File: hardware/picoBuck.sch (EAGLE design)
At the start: 23 parts, among them U1 AL8805, U2 AL8805, U3 AL8805

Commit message: Bringing up to standards- submitting this for review
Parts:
- added FRAME1: FRAME-LETTER, SparkFun-Aesthetics:FRAME-LETTER
- added LOGO1: OSHW-LOGOS, SparkFun-Aesthetics:OSHW-LOGOS
- added LOGO2: LOGO-SFENEW, SparkFun-Aesthetics:LOGO-SFENEW
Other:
- note added: "01"
- note removed: "PicoBuck"
- moved on the sheet: C1, C2, C3, C4, C5, C6, CH1, CH2, CH3, D1, D2, D3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

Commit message: Tweaks on text positions.
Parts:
- removed JP1: (no value), SparkFun:M03SCREW_LOCK
- added JP3, JP4: M022.54MM_SCREWTERM, SparkFun-Connectors:M022.54MM_SCREWTERM
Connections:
- net CTRL_CH1: now also JP4.1; no longer JP1.3
- net CTRL_CH2: now also JP3.2; no longer JP1.2
- net CTRL_CH3: now also JP3.1; no longer JP1.1
- net GND: now also JP4.2
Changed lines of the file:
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@@
 <part name="L3" library="Protofusion" deviceset="SRN6045" device=""/>
 <part name="JP2" library="SparkFun" deviceset="M02" device="3.5MM_LOCK"/>
-<part name="JP1" library="SparkFun" deviceset="M03" device="SCREW_LOCK"/>
 <part name="CH2" library="SparkFun" deviceset="M02" device="3.5MM_LOCK"/>
 <part name="CH1" library="SparkFun" deviceset="M02" device="3.5MM_LOCK"/>
@@
 <part name="LOGO2" library="SparkFun-Aesthetics" deviceset="LOGO-SFE" device="NEW"/>
 <part name="FRAME1" library="SparkFun-Aesthetics" deviceset="FRAME-LETTER" device=""/>
+<part name="JP3" library="SparkFun-Connectors" deviceset="M02" device="2.54MM_SCREWTERM" value="M022.54MM_SCREWTERM"/>
+<part name="JP4" library="SparkFun-Connectors" deviceset="M02" device="2.54MM_SCREWTERM" value="M022.54MM_SCREWTERM"/>
 </parts>
 <sheets>
@@
 <instance part="L3" gate="G$1" x="203.2" y="121.92" rot="R90"/>
 <instance part="JP2" gate="G$1" x="111.76" y="55.88" rot="R180"/>
-<instance part="JP1" gate="G$1" x="111.76" y="68.58" rot="R180"/>
 <instance part="CH2" gate="G$1" x="142.24" y="137.16" rot="R180"/>
 <instance part="CH1" gate="G$1" x="63.5" y="137.16" rot="R180"/>
@@
 <instance part="FRAME1" gate="G$1" x="0" y="0"/>
 <instance part="FRAME1" gate="G$2" x="147.32" y="0"/>
+<instance part="JP3" gate="G$1" x="111.76" y="81.28" smashed="yes" rot="R180">
+<attribute name="NAME" x="114.3" y="75.438" size="1.778" layer="95" rot="R180"/>
+</instance>
+<instance part="JP4" gate="G$1" x="111.76" y="68.58" smashed="yes" rot="R180">
+<attribute name="NAME" x="114.3" y="62.738" size="1.778" layer="95" rot="R180"/>
+</instance>
 </instances>
 <busses>
 </busses>
 <nets>
-<net name="GND" class="1">
+<net name="GND" class="0">
 <segment>
 <pinref part="U2" gate="G$1" pin="GND"/>
@@
 <segment>
 <pinref part="JP2" gate="G$1" pin="1"/>
-<wire x1="104.14" y1="55.88" x2="93.98" y2="55.88" width="0.1524" layer="91"/>
-<label x="93.98" y="55.88" size="1.778" layer="95"/>
-</segment>
-</net>
-<net name="VIN" class="1">
+<wire x1="104.14" y1="55.88" x2="101.6" y2="55.88" width="0.1524" layer="91"/>
+<label x="101.6" y="55.88" size="1.27" layer="95" rot="R180" xref="yes"/>
+</segment>
+<segment>
+<pinref part="JP4" gate="G$1" pin="2"/>
+<wire x1="104.14" y1="66.04" x2="101.6" y2="66.04" width="0.1524" layer="91"/>
+<label x="101.6" y="66.04" size="1.27" layer="95" rot="R180" xref="yes"/>
+</segment>
+</net>
+<net name="VIN" class="0">
 <segment>
 <pinref part="U2" gate="G$1" pin="VIN"/>
@@
 <segment>
 <pinref part="JP2" gate="G$1" pin="2"/>
-<wire x1="104.14" y1="53.34" x2="93.98" y2="53.34" width="0.1524" layer="91"/>
-<label x="93.98" y="53.34" size="1.778" layer="95"/>
+<wire x1="104.14" y1="53.34" x2="101.6" y2="53.34" width="0.1524" layer="91"/>
+<label x="101.6" y="53.34" size="1.27" layer="95" rot="R180" xref="yes"/>
 </segment>
 </net>
@@
 <net name="CTRL_CH1" class="0">
 <segment>
-<pinref part="JP1" gate="G$1" pin="3"/>
-<wire x1="104.14" y1="66.04" x2="93.98" y2="66.04" width="0.1524" layer="91"/>
-<label x="91.44" y="66.04" size="1.778" layer="95"/>
-</segment>
-<segment>
 <pinref part="U1" gate="G$1" pin="CTRL"/>
 <wire x1="17.78" y1="157.48" x2="5.08" y2="157.48" width="0.1524" layer="91"/>
 <label x="5.08" y="157.48" size="1.778" layer="95"/>
 </segment>
+<segment>
+<pinref part="JP4" gate="G$1" pin="1"/>
+<wire x1="104.14" y1="68.58" x2="101.6" y2="68.58" width="0.1524" layer="91"/>
+<label x="101.6" y="68.58" size="1.27" layer="95" rot="R180" xref="yes"/>
+</segment>
 </net>
 <net name="CTRL_CH2" class="0">
-<segment>
-<pinref part="JP1" gate="G$1" pin="2"/>
-<wire x1="104.14" y1="68.58" x2="93.98" y2="68.58" width="0.1524" layer="91"/>
-<label x="91.44" y="68.58" size="1.778" layer="95"/>
-</segment>
 <segment>
 <pinref part="U2" gate="G$1" pin="CTRL"/>
@@
 <label x="83.82" y="157.48" size="1.778" layer="95"/>
 </segment>
+<segment>
+<pinref part="JP3" gate="G$1" pin="2"/>
+<wire x1="104.14" y1="78.74" x2="101.6" y2="78.74" width="0.1524" layer="91"/>
+<label x="101.6" y="78.74" size="1.27" layer="95" rot="R180" xref="yes"/>
+</segment>
 </net>
 <net name="CTRL_CH3" class="0">
-<segment>
-<pinref part="JP1" gate="G$1" pin="1"/>
-<wire x1="104.14" y1="71.12" x2="93.98" y2="71.12" width="0.1524" layer="91"/>
-<label x="91.44" y="71.12" size="1.778" layer="95"/>
-</segment>
 <segment>
 <pinref part="U3" gate="G$1" pin="CTRL"/>
@@
 <label x="162.56" y="160.02" size="1.778" layer="95"/>
 </segment>
-</net>
+<segment>
+<pinref part="JP3" gate="G$1" pin="1"/>
+<wire x1="104.14" y1="81.28" x2="101.6" y2="81.28" width="0.1524" layer="91"/>
+<label x="101.6" y="81.28" size="1.27" layer="95" rot="R180" xref="yes"/>
+</segment>
+</net>

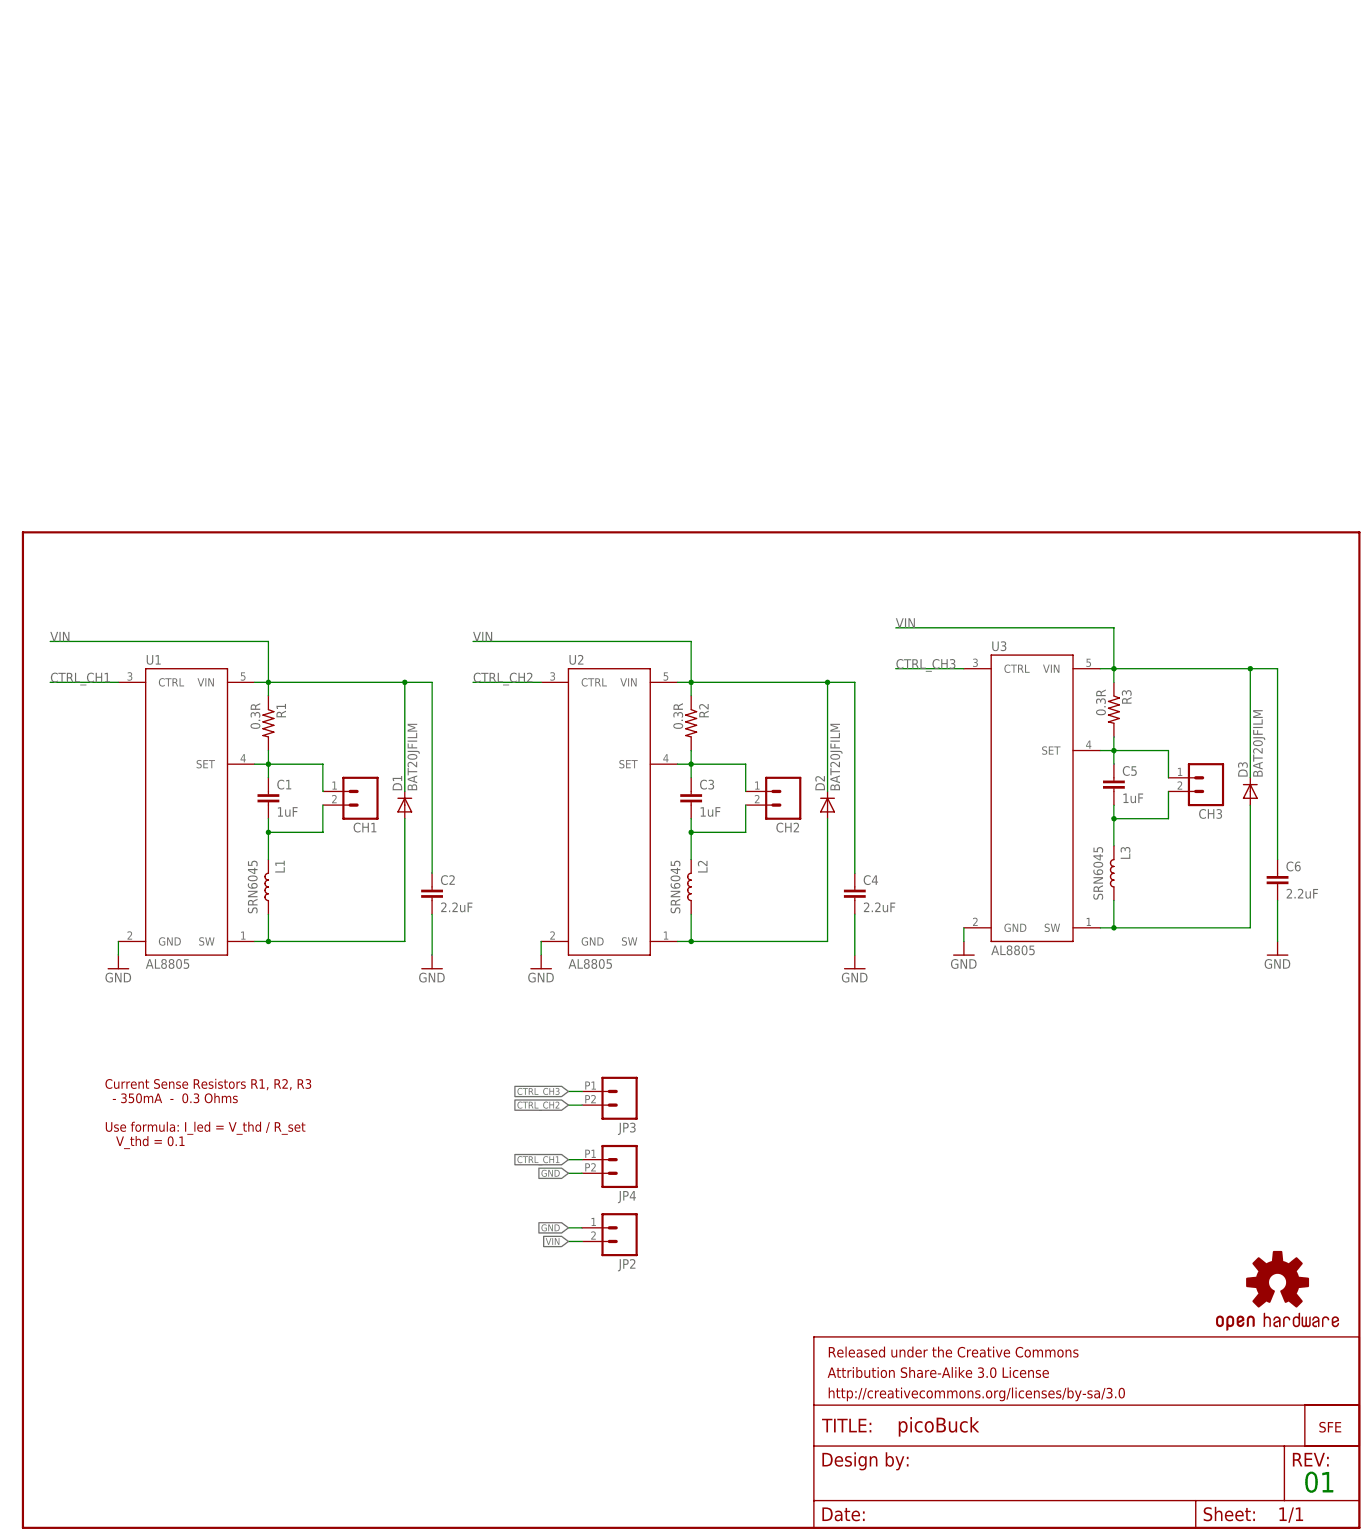
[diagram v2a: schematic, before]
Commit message: Update to v10, for release. Add .gitignore and README
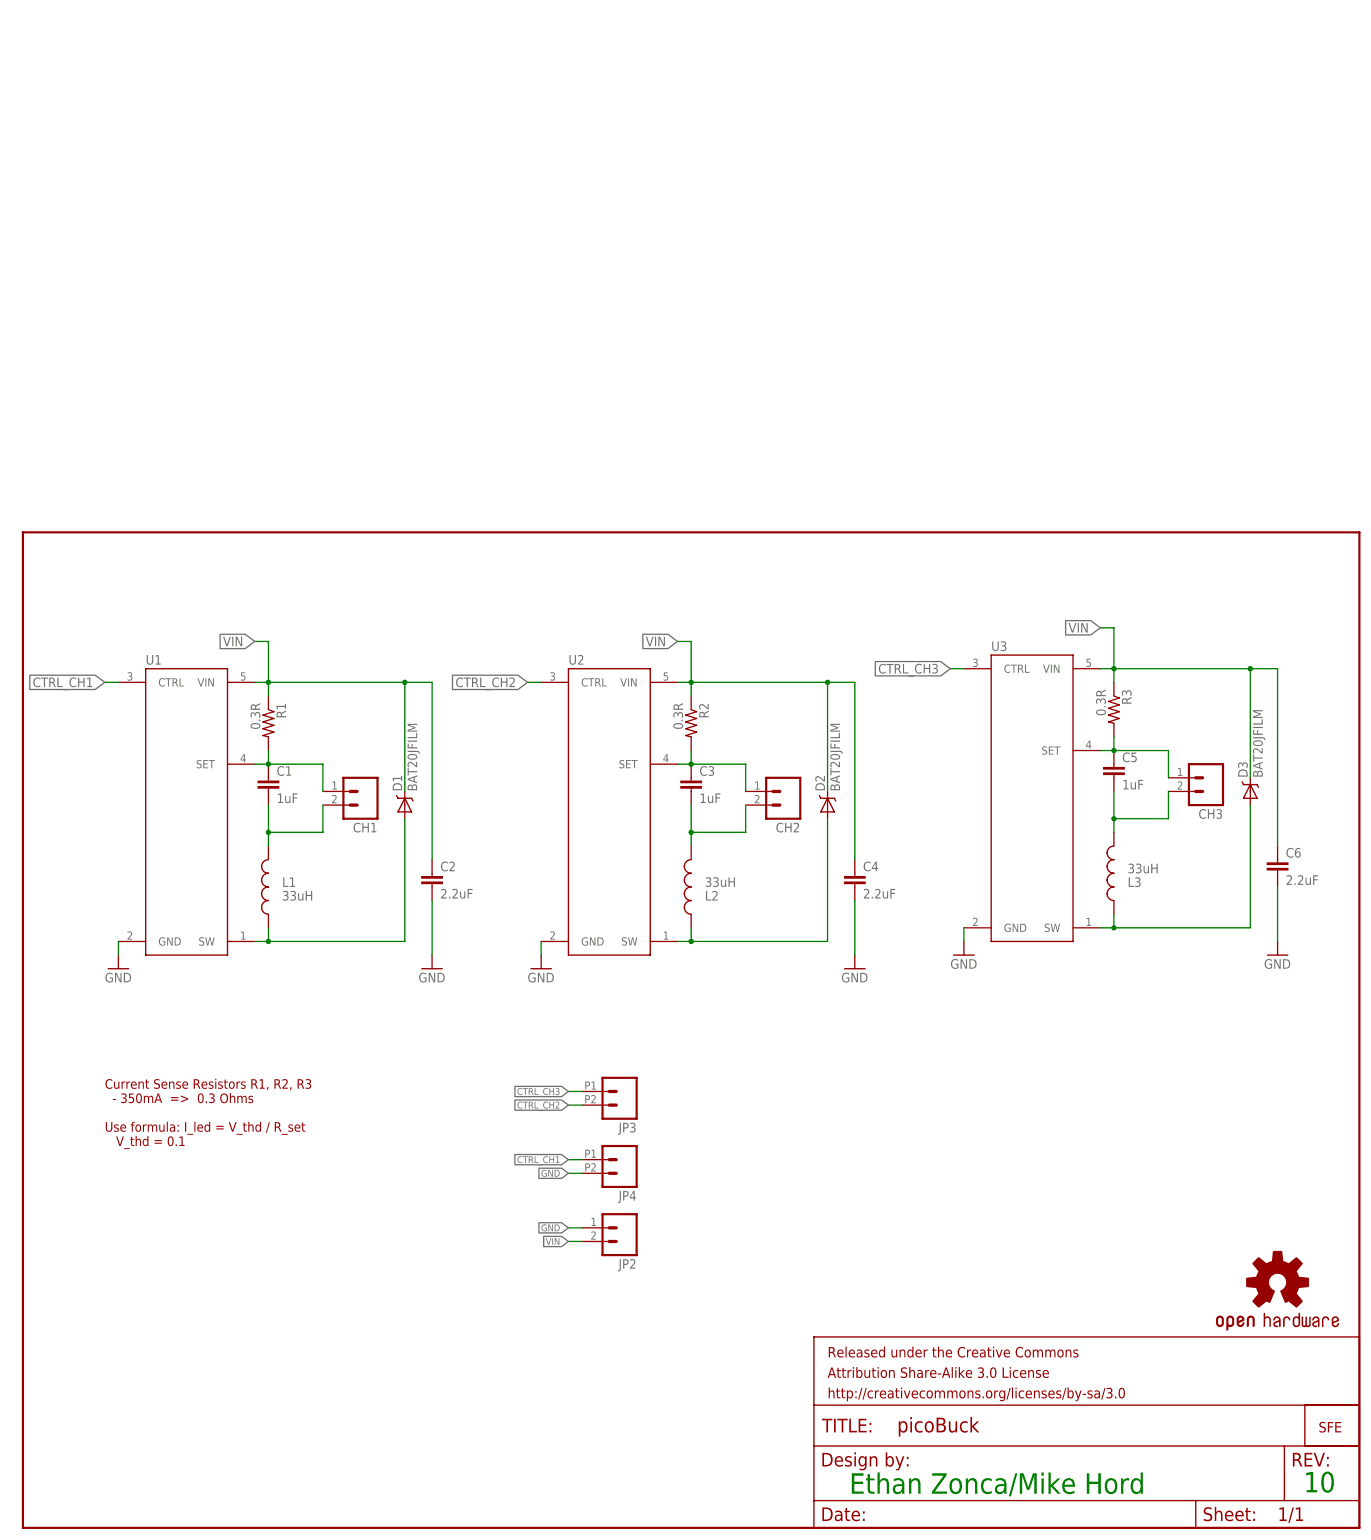
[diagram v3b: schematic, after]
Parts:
- C1, C3, C5: device resistor:C-EUC0805 -> SparkFun-Capacitors:1.0UF-25V-+80/-20(0805)
- C2, C4, C6: device resistor:C-EUC0805 -> SparkFun-Capacitors:2.2UF-25V-+80/-20(0805)
- D1, D2, D3: device SparkFun:DIODESOD -> SparkFun-DiscreteSemi:BAT20JFILM
- L1, L2, L3: value SRN6045 -> 33uH; device Protofusion:SRN6045 -> SparkFun-Passives:INDUCTORBOURNS_SRN6045
- R1, R2, R3: device resistor:R-US_R0805 -> SparkFun-Resistors:0.3OHM-1/8W-1%(0805)
- U1, U2, U3: value AL8805 -> (none); device Protofusion:AL8805 -> SparkFun-PowerIC:AL8805
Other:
- note added: "10"
- note added: "Current Sense Resistors R1, R2, R3 - 350mA => 0.3 Ohms Use formula: I_led = V_thd / R_set V_thd = 0.1"
- note added: "Ethan Zonca/Mike Hord"
- note removed: "01"
- note removed: "Current Sense Resistors R1, R2, R3 - 350mA - 0.3 Ohms Use formula: I_led = V_thd / R_set V_thd = 0.1"
- moved on the sheet: C1, C2, C3, C4, C5, C6, L1, L2, L3

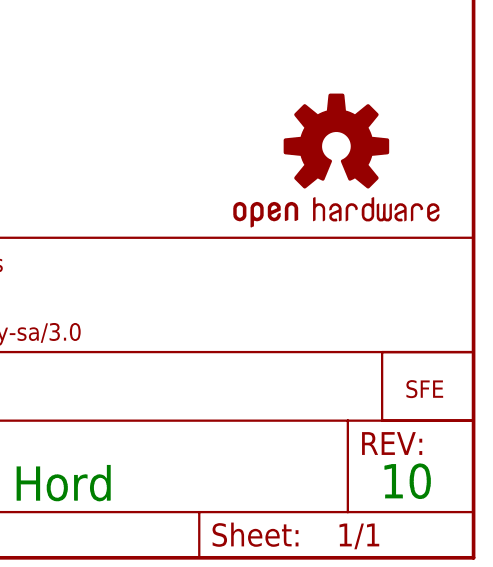
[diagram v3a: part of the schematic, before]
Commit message: Production ready
panelized and added fiducials
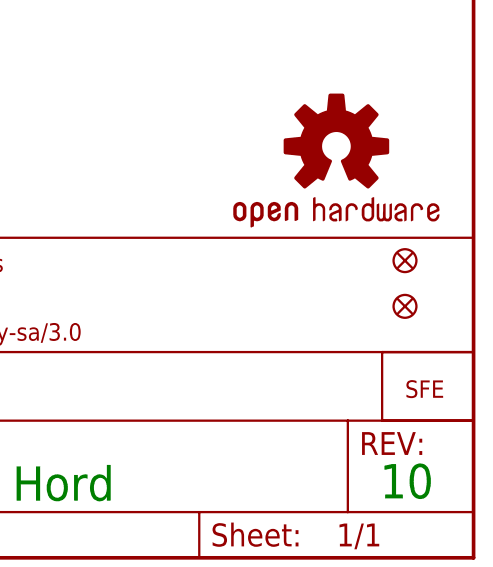
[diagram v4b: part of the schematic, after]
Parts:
- added FID1, FID2: FIDUCIALUFIDUCIAL, SparkFun-Aesthetics:FIDUCIALUFIDUCIAL
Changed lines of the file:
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@@
 <part name="JP3" library="SparkFun-Connectors" deviceset="M02" device="2.54MM_SCREWTERM" value="M022.54MM_SCREWTERM"/>
 <part name="JP4" library="SparkFun-Connectors" deviceset="M02" device="2.54MM_SCREWTERM" value="M022.54MM_SCREWTERM"/>
+<part name="FID1" library="SparkFun-Aesthetics" deviceset="FIDUCIAL" device="UFIDUCIAL"/>
+<part name="FID2" library="SparkFun-Aesthetics" deviceset="FIDUCIAL" device="UFIDUCIAL"/>
 </parts>
 <sheets>
@@
 <attribute name="NAME" x="114.3" y="62.738" size="1.778" layer="95" rot="R180"/>
 </instance>
+<instance part="FID1" gate="G$1" x="241.3" y="33.02"/>
+<instance part="FID2" gate="G$1" x="241.3" y="27.94"/>
 </instances>
 <busses>
